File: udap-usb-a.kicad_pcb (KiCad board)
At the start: 2 copper layers, 25 x 10 mm, 25 parts, among them J201 Conn_02x04_Counter_Clockwise, P1 USB_C_Plug, U2 MIC5245-3.3YM5, U201 NUF6401MNT1, U202 STM32F042F6Px, U4 NUF2042XV6T1G

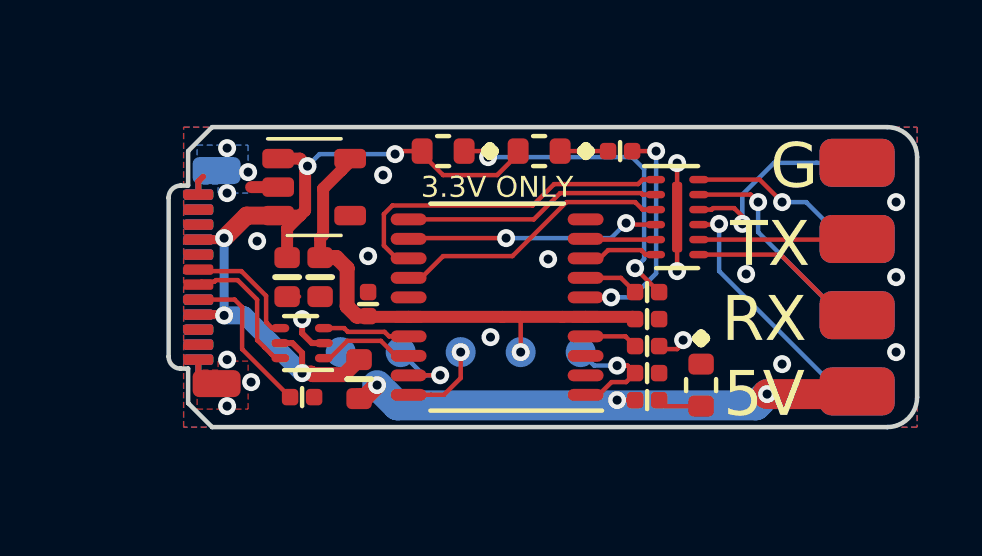
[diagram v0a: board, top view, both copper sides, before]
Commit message: Update PCB for USB-A version
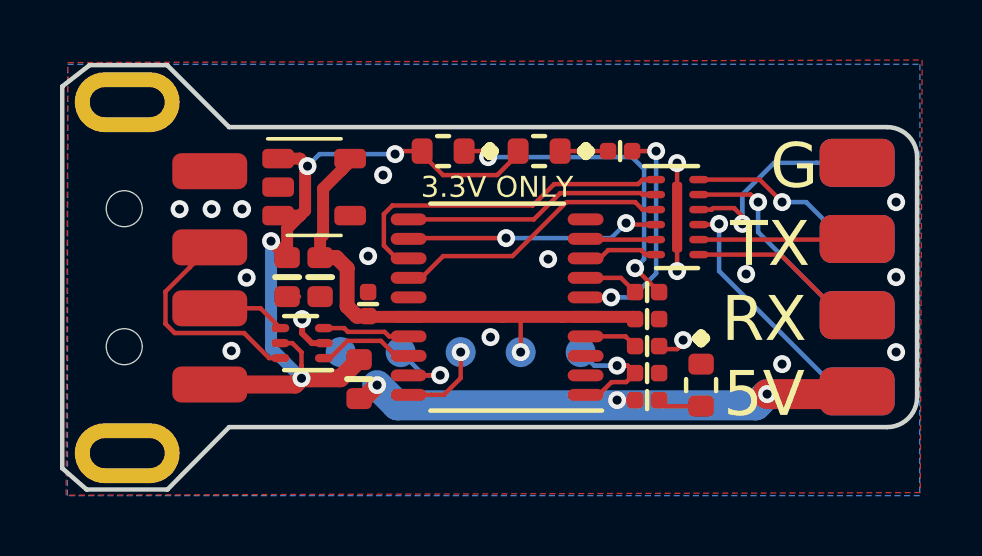
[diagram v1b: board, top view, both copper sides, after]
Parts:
- removed P1: USB_C_Plug, usb:USB_C_Plug_Molex_1054440001
- removed R3: 5.1k, passive:R_0402
- added P101: USB_A, usb:USB_A_1001-011-01101, F.Cu at (90.2, 106.0)
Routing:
- net Net-(P1-PadA5): track 5.23 -> 0.00 mm
- net GND: track 11.5 -> 6.37 mm, vias 20 -> 18
- net /DP: track 4.67 -> 7.46 mm
- net +5V: track 28.1 -> 25.7 mm, vias 5 -> 4
- net /DM: track 4.05 -> 2.63 mm
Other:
- board size 25 x 10 mm -> 28.5 x 14.1 mm

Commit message: Spaced 4.7u apart more, now easier to solder
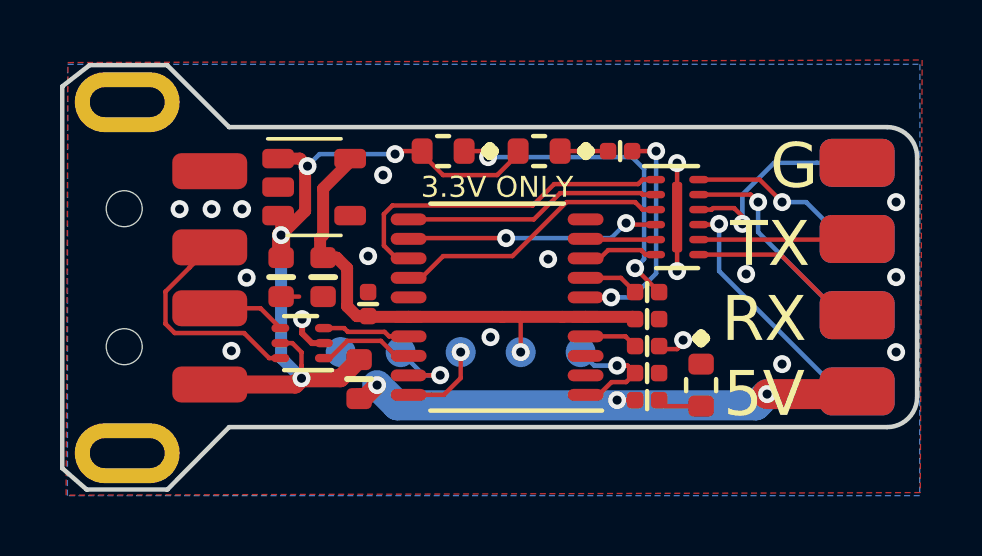
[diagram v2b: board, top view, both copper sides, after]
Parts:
- moved C2 0.20 mm to (93.3, 106.0)
- moved C5 0.10 mm to (94.7, 106.0)
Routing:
- net +5V: track 25.7 -> 25.1 mm
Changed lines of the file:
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@@
   )
   (module passive:C_0603 (layer F.Cu)
-    (at 94.6 106 270)
+    (at 94.7 106 270)
     (descr "Capacitor SMD 0603 (1608 Metric), square (rectangular) end terminal, IPC_7351 nominal, (Body size source: http://www.tortai-tech.com/upload/download/2011102023233369053.pdf), generated with kicad-footprint-generator")
     (tags capacitor)
@@
   )
   (module passive:C_0603 (layer F.Cu)
-    (at 93.5 106 270)
+    (at 93.3 106 270)
     (descr "Capacitor SMD 0603 (1608 Metric), square (rectangular) end terminal, IPC_7351 nominal, (Body size source: http://www.tortai-tech.com/upload/download/2011102023233369053.pdf), generated with kicad-footprint-generator")
     (tags capacitor)
@@
   (segment (start 105.025 107.325) (end 105.1 107.4) (width 0.4) (layer F.Cu) (net 1))
   (segment (start 103.45 107.325) (end 105.025 107.325) (width 0.4) (layer F.Cu) (net 1))
-  (segment (start 94.7 104.6) (end 94.7 103.05) (width 0.4) (layer F.Cu) (net 1))
-  (segment (start 94.7 103.05) (end 95.30429 102.44571) (width 0.4) (layer F.Cu) (net 1))
-  (segment (start 94.6 105.35) (end 94.6 104.7) (width 0.4) (layer F.Cu) (net 1))
-  (segment (start 95.30429 102.44571) (end 95.7 102.05) (width 0.4) (layer F.Cu) (net 1))
-  (segment (start 94.6 104.7) (end 94.7 104.6) (width 0.4) (layer F.Cu) (net 1))
-  (segment (start 95.825 107.3) (end 96.2 107.3) (width 0.5) (layer F.Cu) (net 1))
-  (segment (start 95.5 106.975) (end 95.825 107.3) (width 0.5) (layer F.Cu) (net 1))
-  (segment (start 94.6 105.35) (end 95.15 105.35) (width 0.5) (layer F.Cu) (net 1))
-  (segment (start 95.5 105.7) (end 95.5 106.975) (width 0.5) (layer F.Cu) (net 1))
-  (segment (start 95.15 105.35) (end 95.5 105.7) (width 0.5) (layer F.Cu) (net 1))
   (segment (start 101.2855 107.3307) (end 101.2798 107.325) (width 0.15) (layer F.Cu) (net 1))
   (segment (start 101.2855 108.5) (end 101.2855 107.3307) (width 0.15) (layer F.Cu) (net 1))
   (segment (start 100.675 107.325) (end 101.2798 107.325) (width 0.4) (layer F.Cu) (net 1))
   (segment (start 101.2798 107.325) (end 102.675 107.325) (width 0.4) (layer F.Cu) (net 1))
+  (segment (start 95.5 106.975) (end 95.825 107.3) (width 0.4) (layer F.Cu) (net 1))
+  (segment (start 95.5 105.7) (end 95.5 106.975) (width 0.4) (layer F.Cu) (net 1))
+  (segment (start 95.15 105.35) (end 95.5 105.7) (width 0.4) (layer F.Cu) (net 1))
+  (segment (start 94.7 103.05) (end 94.7 104.6) (width 0.4) (layer F.Cu) (net 1))
+  (segment (start 95.825 107.3) (end 96.2 107.3) (width 0.4) (layer F.Cu) (net 1))
+  (segment (start 94.6 105.35) (end 95.15 105.35) (width 0.4) (layer F.Cu) (net 1))
+  (segment (start 95.7 102.05) (end 94.7 103.05) (width 0.4) (layer F.Cu) (net 1))
+  (segment (start 94.7 104.6) (end 94.6 104.7) (width 0.4) (layer F.Cu) (net 1))
+  (segment (start 94.6 104.7) (end 94.6 105.35) (width 0.4) (layer F.Cu) (net 1))
   (segment (start 94 107.875) (end 94 107.4) (width 0.2) (layer F.Cu) (net 2))
   (via (at 94 107.4) (size 0.6) (drill 0.3) (layers F.Cu B.Cu) (net 2))
@@
   (segment (start 93.93 102.05) (end 93.3 102.05) (width 0.4) (layer F.Cu) (net 3))
   (segment (start 94.18001 102.30001) (end 93.93 102.05) (width 0.4) (layer F.Cu) (net 3))
-  (segment (start 93.3 103.95) (end 93.93 103.95) (width 0.4) (layer F.Cu) (net 3))
   (segment (start 98 101.9) (end 98 101.8) (width 0.15) (layer F.Cu) (net 3))
   (segment (start 98.7 102.6) (end 98 101.9) (width 0.15) (layer F.Cu) (net 3))
@@
   (segment (start 94.18001 102.31999) (end 94.18001 102.30001) (width 0.4) (layer F.Cu) (net 3))
   (segment (start 94.1 102.4) (end 94.18001 102.31999) (width 0.4) (layer F.Cu) (net 3))
-  (segment (start 93.93 103.95) (end 94.1 103.78) (width 0.4) (layer F.Cu) (net 3))
   (segment (start 94.1 103.78) (end 94.1 102.4) (width 0.4) (layer F.Cu) (net 3))
-  (segment (start 93.5 104.38) (end 93.93 103.95) (width 0.4) (layer F.Cu) (net 3))
-  (segment (start 93.5 105.35) (end 93.5 104.38) (width 0.4) (layer F.Cu) (net 3))
   (via (at 93.98 109.3724) (size 0.6) (drill 0.3) (layers F.Cu B.Cu) (net 3))
   (segment (start 95.9 108.75) (end 95.2776 109.3724) (width 0.6) (layer F.Cu) (net 3))
@@
   (segment (start 93.675 108.2) (end 93.98 108.505) (width 0.15) (layer F.Cu) (net 3))
   (segment (start 93.275 108.2) (end 93.675 108.2) (width 0.15) (layer F.Cu) (net 3))
-  (via (at 92.964 104.8004) (size 0.6) (drill 0.3) (layers F.Cu B.Cu) (net 3))
-  (segment (start 93.5 105.35) (end 93.5 105.3364) (width 0.4) (layer F.Cu) (net 3))
-  (segment (start 93.5 105.3364) (end 92.964 104.8004) (width 0.4) (layer F.Cu) (net 3))
-  (segment (start 92.964 108.3564) (end 92.964 104.8004) (width 0.4) (layer B.Cu) (net 3))
-  (segment (start 93.98 109.3724) (end 92.964 108.3564) (width 0.4) (layer B.Cu) (net 3))
   (segment (start 93.7728 109.5796) (end 93.98 109.3724) (width 0.6) (layer F.Cu) (net 3))
   (segment (start 90.92 109.5796) (end 93.7728 109.5796) (width 0.6) (layer F.Cu) (net 3))
+  (via (at 93.300006 104.6) (size 0.6) (drill 0.3) (layers F.Cu B.Cu) (net 3))
+  (segment (start 93.300006 108.692406) (end 93.300006 105.024264) (width 0.4) (layer B.Cu) (net 3))
+  (segment (start 93.300006 105.024264) (end 93.300006 104.6) (width 0.4) (layer B.Cu) (net 3))
+  (segment (start 93.98 109.3724) (end 93.300006 108.692406) (width 0.4) (layer B.Cu) (net 3))
+  (segment (start 93.3 104.600006) (end 93.300006 104.6) (width 0.6) (layer F.Cu) (net 3))
+  (segment (start 93.3 105.35) (end 93.3 104.600006) (width 0.6) (layer F.Cu) (net 3))
+  (segment (start 93.3 104.599994) (end 93.300006 104.6) (width 0.4) (layer F.Cu) (net 3))
+  (segment (start 93.3 103.95) (end 93.3 104.599994) (width 0.4) (layer F.Cu) (net 3))
+  (segment (start 94.1 103.800006) (end 93.300006 104.6) (width 0.4) (layer F.Cu) (net 3))
+  (segment (start 94.1 103.78) (end 94.1 103.800006) (width 0.4) (layer F.Cu) (net 3))
   (segment (start 92.6146 107.0396) (end 93.275 107.7) (width 0.15) (layer F.Cu) (net 4))
   (segment (start 90.92 107.0396) (end 92.6146 107.0396) (width 0.15) (layer F.Cu) (net 4))

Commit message: Add JLCPCB Order Number placeholder
This adds silkscreen under the MCU saying "JLCJLCJLCJLC". When ordering
with JLCPCB, they'll replace this with the order number. If this isn't
done, the order number will be placed somewhere random where it can
potentially be seen after assembly.

Since this is purely for a slight convenience when using JLCPCB, I can
also see just not doing this.

Also see:
https://support.jlcpcb.com/article/28-how-to-put-jlc-production-id-at-a-specified-area-on-the-pcb
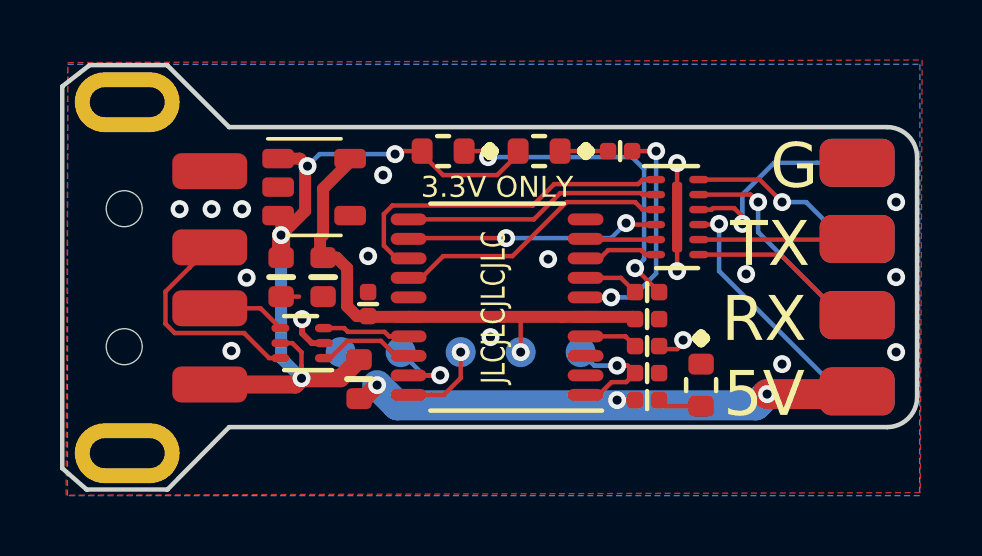
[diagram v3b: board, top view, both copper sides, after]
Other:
- board text added: "JLCJLCJLCJLC"
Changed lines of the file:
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@@
   (general
     (thickness 0.7)
-    (drawings 28)
+    (drawings 29)
     (tracks 230)
     (zones 0)
@@
     )
   )
+  (gr_text JLCJLCJLCJLC (at 100.3808 107.0102 90) (layer F.SilkS)
+    (effects (font (size 0.8 0.6) (thickness 0.15)))
+  )
   (gr_line (start 86.8172 113.0808) (end 86.0044 112.3696) (layer Edge.Cuts) (width 0.15))
